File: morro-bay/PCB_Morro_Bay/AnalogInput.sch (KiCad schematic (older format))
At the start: 50 parts, among them U5 LM2902, U6 LM2902, U7 LM2902, U8 LM2902, U9 LM2902

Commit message: Work on analog inputs and pin naming
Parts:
- removed unit 2 of U9
- removed unit 3 of U9
- removed unit 4 of U9
- added D1, D10, D11, D12, D13, D14, D15, D16, D17, D18, D19, D2, D20, D3, D4, D5, D6, D7, D8, D9: 3.3V, symbol Device:D_Zener
- added R49, R51, R57, R59, R63, R65: 51.1K, symbol Device:R_US
- added R50, R52, R58, R60, R64, R66: 100K, symbol Device:R_US
- added R53, R54, R55, R56, R61, R62, R67, R68: 1K, symbol Device:R_US
- added SW1, SW10, SW11, SW12, SW13, SW14, SW15, SW16, SW17, SW18, SW19, SW2, SW20, SW3, SW4, SW5, SW6, SW7, SW8, SW9: SW_SPST, symbol Switch:SW_SPST
- added U10, U11, U12: LM2902, symbol Amplifier_Operational:LM2902
- R10, R12, R14, R16, R22, R24, R26, R28, R34, R36, R38, R40, R46, R48: value 10K -> 100K
- R11, R13, R15, R21, R23, R25, R27, R33, R35, R37, R39, R45, R47, R9: value 5.1K -> 51.1K
- R17, R19, R29, R31, R41, R43: value 5.1K -> 1K; Tolerance 0.1% -> (none)
- R18, R20, R30, R32, R42, R44: value 10K -> 1K; Tolerance 0.1% -> (none)
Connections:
- net labels added: 3V3_IN_1, 3V3_IN_10, 3V3_IN_11, 3V3_IN_12, 3V3_IN_13, 3V3_IN_14, 3V3_IN_15, 3V3_IN_16, 3V3_IN_17, 3V3_IN_18, 3V3_IN_19, 3V3_IN_2, 3V3_IN_20, 3V3_IN_3, 3V3_IN_4, 3V3_IN_5, 3V3_IN_6, 3V3_IN_7, 3V3_IN_8, 3V3_IN_9, 5V_IN_10, 5V_IN_11, 5V_IN_12, 5V_IN_13, 5V_IN_14, 5V_IN_15, 5V_IN_16, 5V_IN_17, 5V_IN_18, 5V_IN_19, 5V_IN_20, 5V_IN_5, 5V_IN_6, 5V_IN_7, 5V_IN_8, 5V_IN_9, IN_10_BUFFERED, IN_11_BUFFERED, IN_12_BUFFERED, IN_13_BUFFERED, IN_14_BUFFERED, IN_15_BUFFERED, IN_16_BUFFERED, IN_17_BUFFERED, IN_18_BUFFERED, IN_19_BUFFERED, IN_1_BUFFERED, IN_20_BUFFERED, IN_2_BUFFERED, IN_3_BUFFERED, IN_4_BUFFERED, IN_5_BUFFERED, IN_6_BUFFERED, IN_7_BUFFERED, IN_8_BUFFERED, IN_9_BUFFERED, SAMD_ADC_10, SAMD_ADC_11, SAMD_ADC_12, SAMD_ADC_13, SAMD_ADC_14, SAMD_ADC_15, SAMD_ADC_16, SAMD_ADC_17, SAMD_ADC_18, SAMD_ADC_19, SAMD_ADC_20, SAMD_ADC_5, SAMD_ADC_6, SAMD_ADC_7, SAMD_ADC_8, SAMD_ADC_9
- wire segments 220 -> 380
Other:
- moved on the sheet: R10, R9, U5A

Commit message: Add input connectors, DIP switches
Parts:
- removed SW1, SW10, SW11, SW12, SW13, SW14, SW15, SW16, SW17, SW18, SW19, SW2, SW20, SW3, SW4, SW5, SW6, SW7, SW8, SW9: SW_SPST, symbol Switch:SW_SPST
- added SW1, SW2: SW_DIP_x10, symbol Switch:SW_DIP_x10
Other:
- note added: "Analog Connectors"
- moved on the sheet: C22, C23, C24, C25, C26, D1, D10, D11, D12, D13, D14, D15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

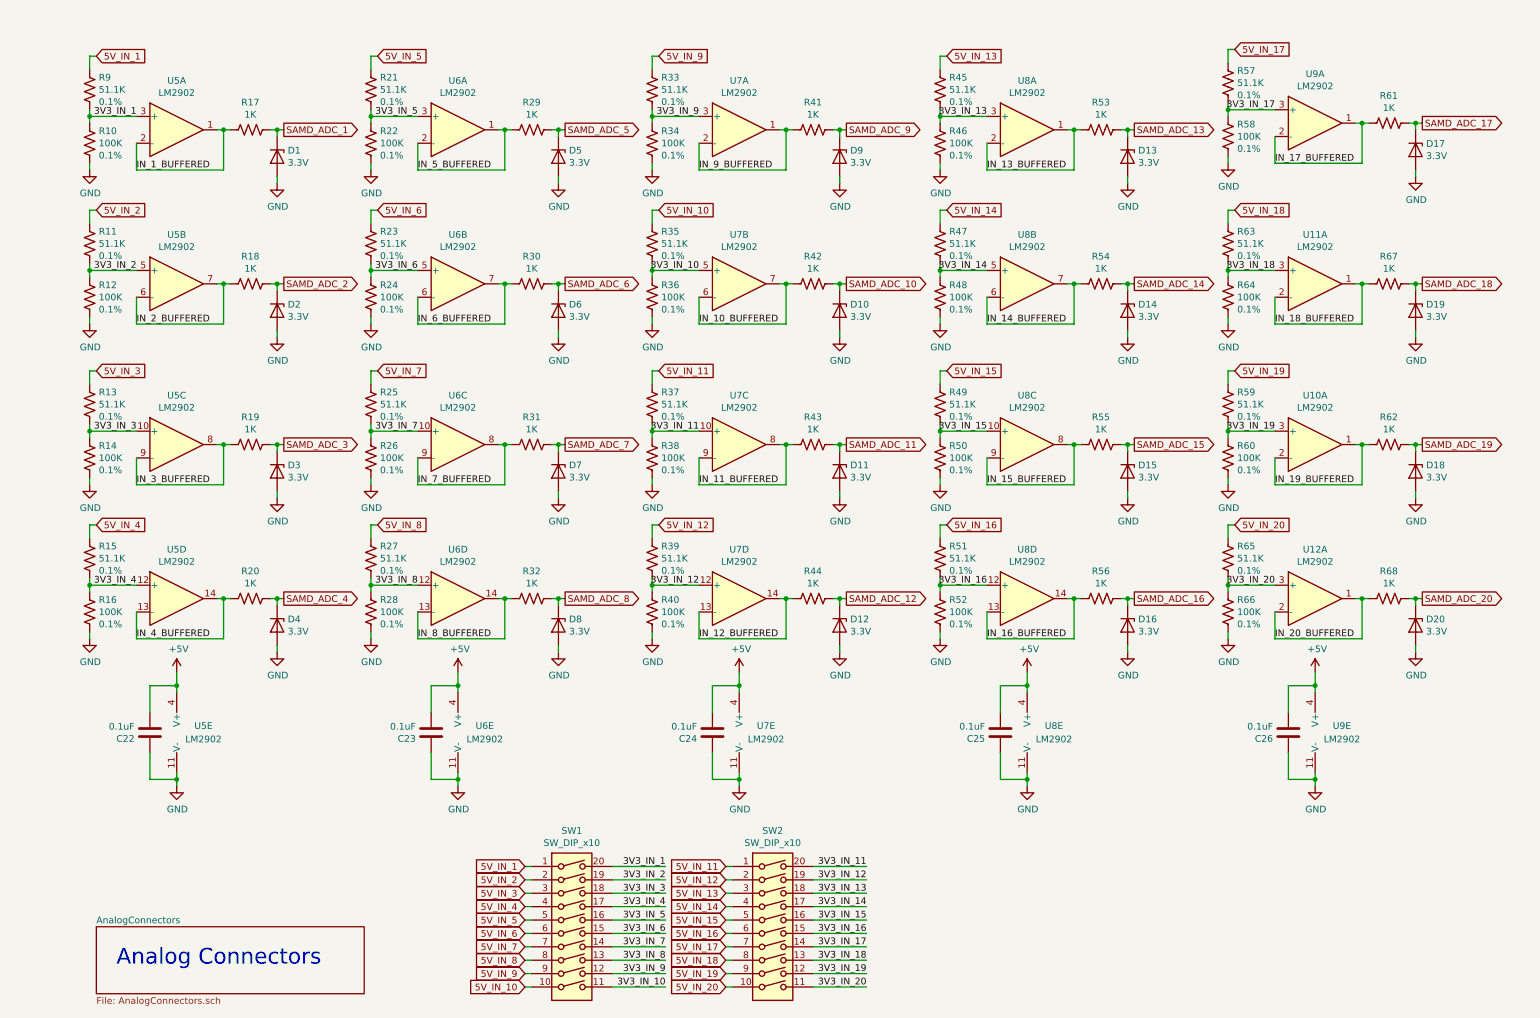
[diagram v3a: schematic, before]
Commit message: Switch to DC-DC reg
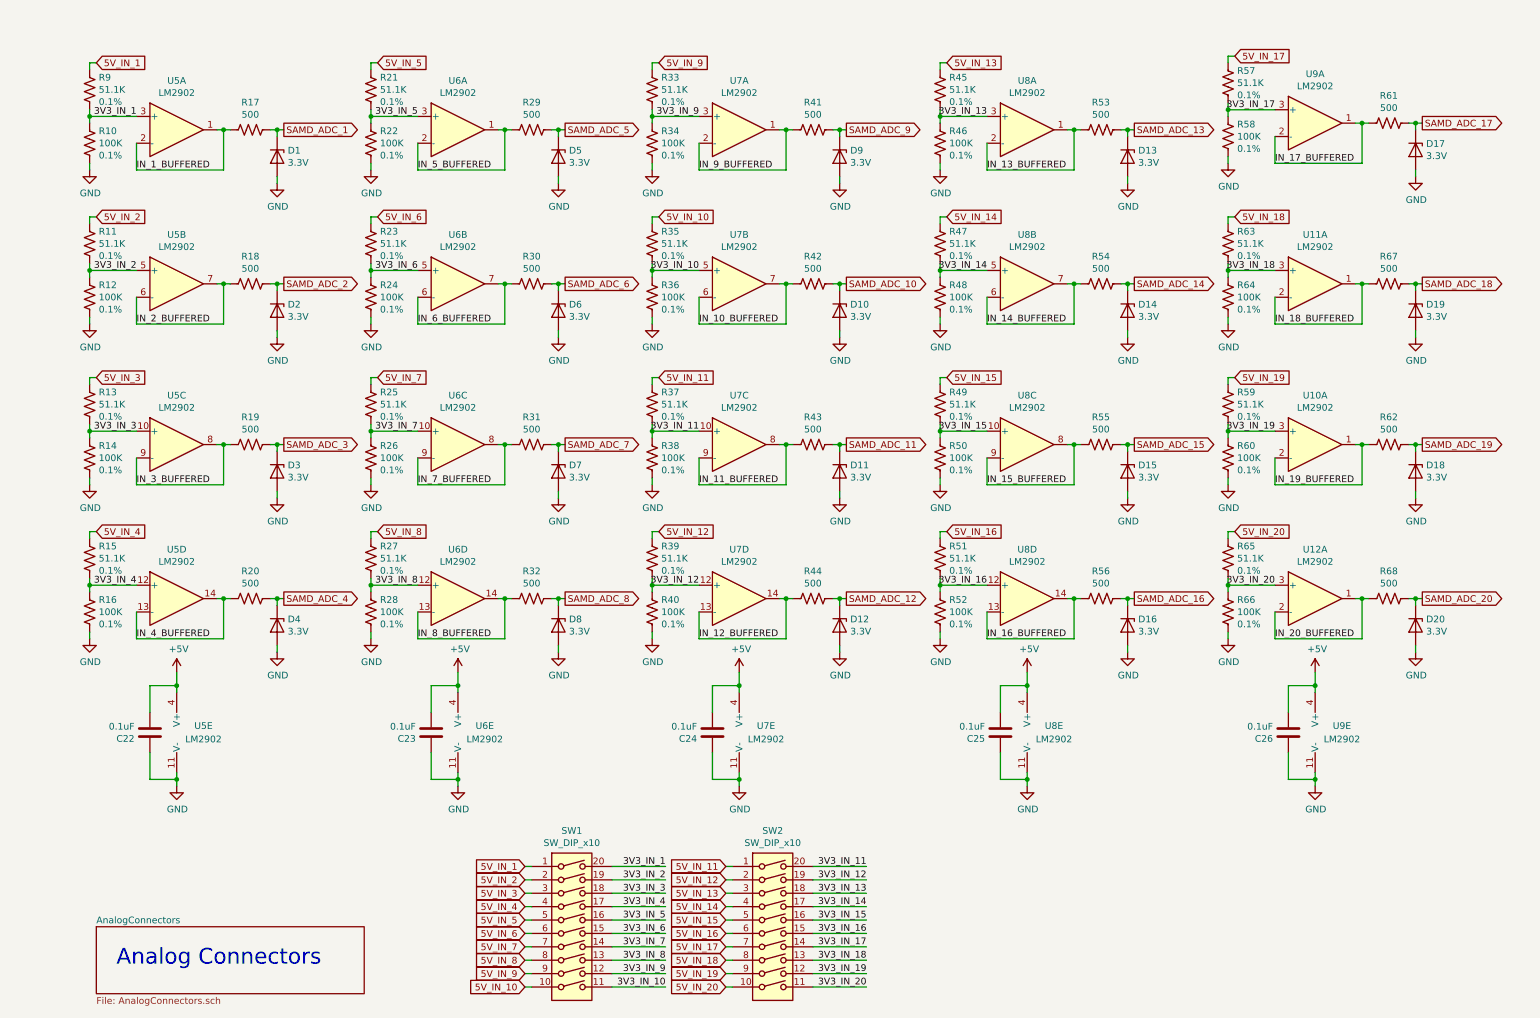
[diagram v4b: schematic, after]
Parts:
- R17, R18, R19, R20, R29, R30, R31, R32, R41, R42, R43, R44, R53, R54, R55, R56, R61, R62, R67, R68: value 1K -> 500

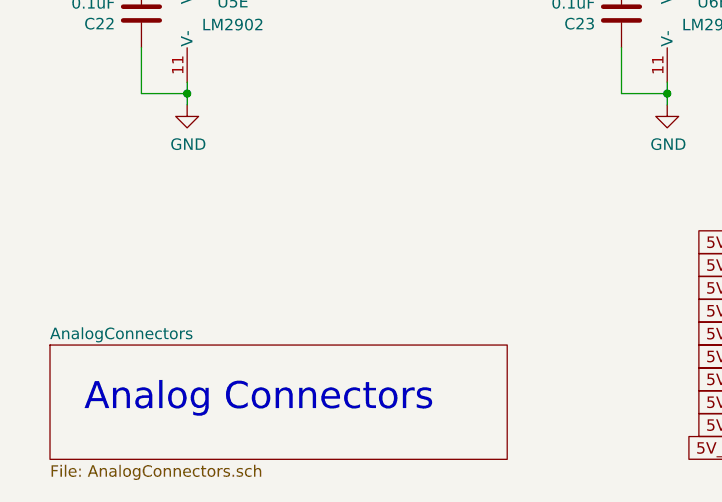
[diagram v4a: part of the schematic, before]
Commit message: Add external ADC
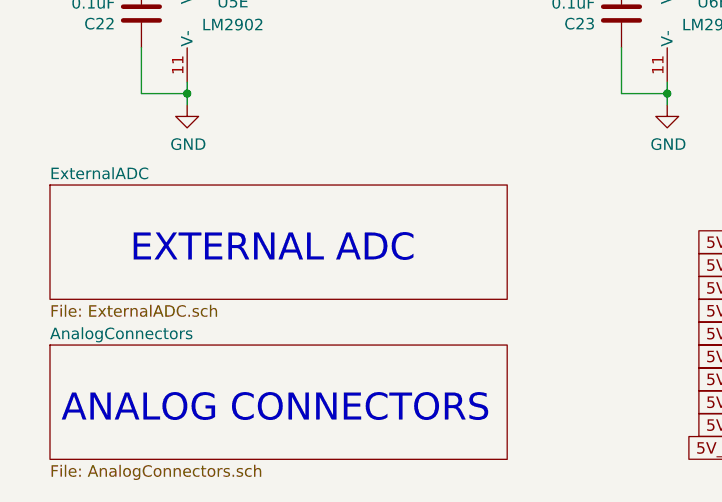
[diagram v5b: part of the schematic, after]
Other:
- note added: "ANALOG CONNECTORS"
- note added: "EXTERNAL ADC"
- note removed: "Analog Connectors"
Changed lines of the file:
@@
 $Descr A4 11693 8268
 encoding utf-8
-Sheet 2 3
+Sheet 2 4
 Title "Morro Bay Data Acquisition Board"
 Date ""
@@
 F1 "AnalogConnectors.sch" 50
 $EndSheet
-Text Notes 800  7400 0    118  ~ 0
-Analog Connectors
+Text Notes 700  7450 0    118  ~ 0
+ANALOG CONNECTORS
 $Comp
 L Switch:SW_DIP_x10 SW1
@@
 Wire Wire Line
 	5350 7550 5400 7550
+$Sheet
+S 650  6400 2000 500
+U 5E5467E7
+F0 "ExternalADC" 50
+F1 "ExternalADC.sch" 50
+$EndSheet
+Text Notes 1000 6750 0    118  ~ 0
+EXTERNAL ADC
 $EndSCHEMATC

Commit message: Ready for initial sch review
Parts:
- added C? (x2): 22uF, symbol Device:CP1
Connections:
- net +5V: now also C?.1, C?.1
- net GND: now also C?.2, C?.2
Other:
- moved on the sheet: SW1, SW2

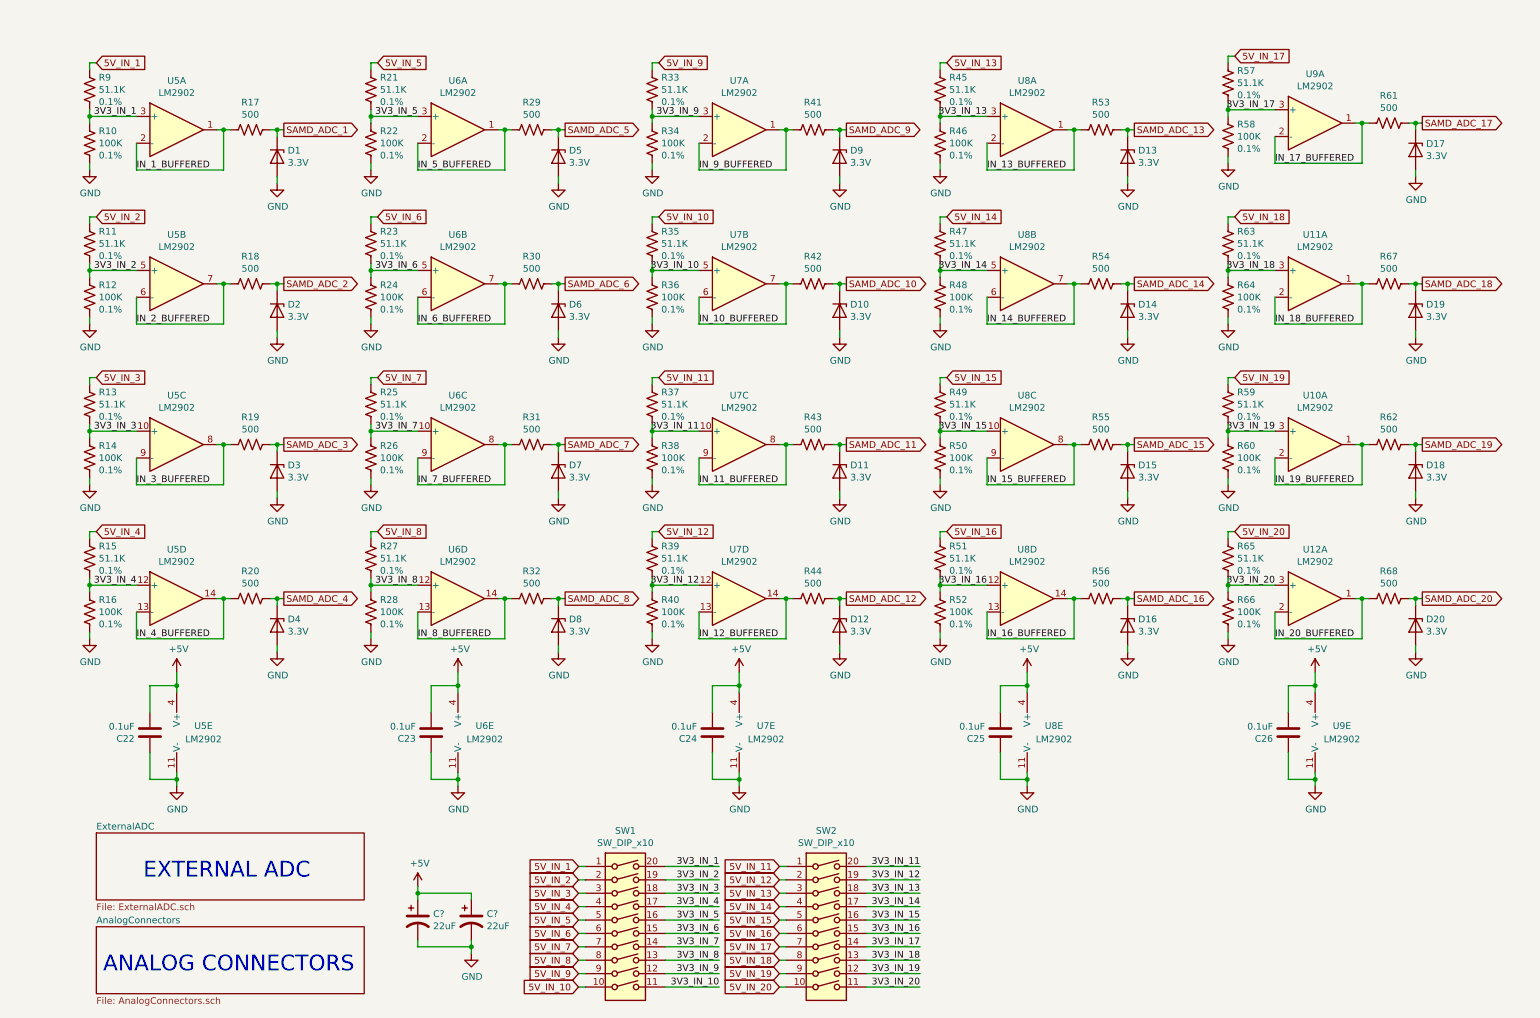
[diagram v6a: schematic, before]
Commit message: Work on BOM
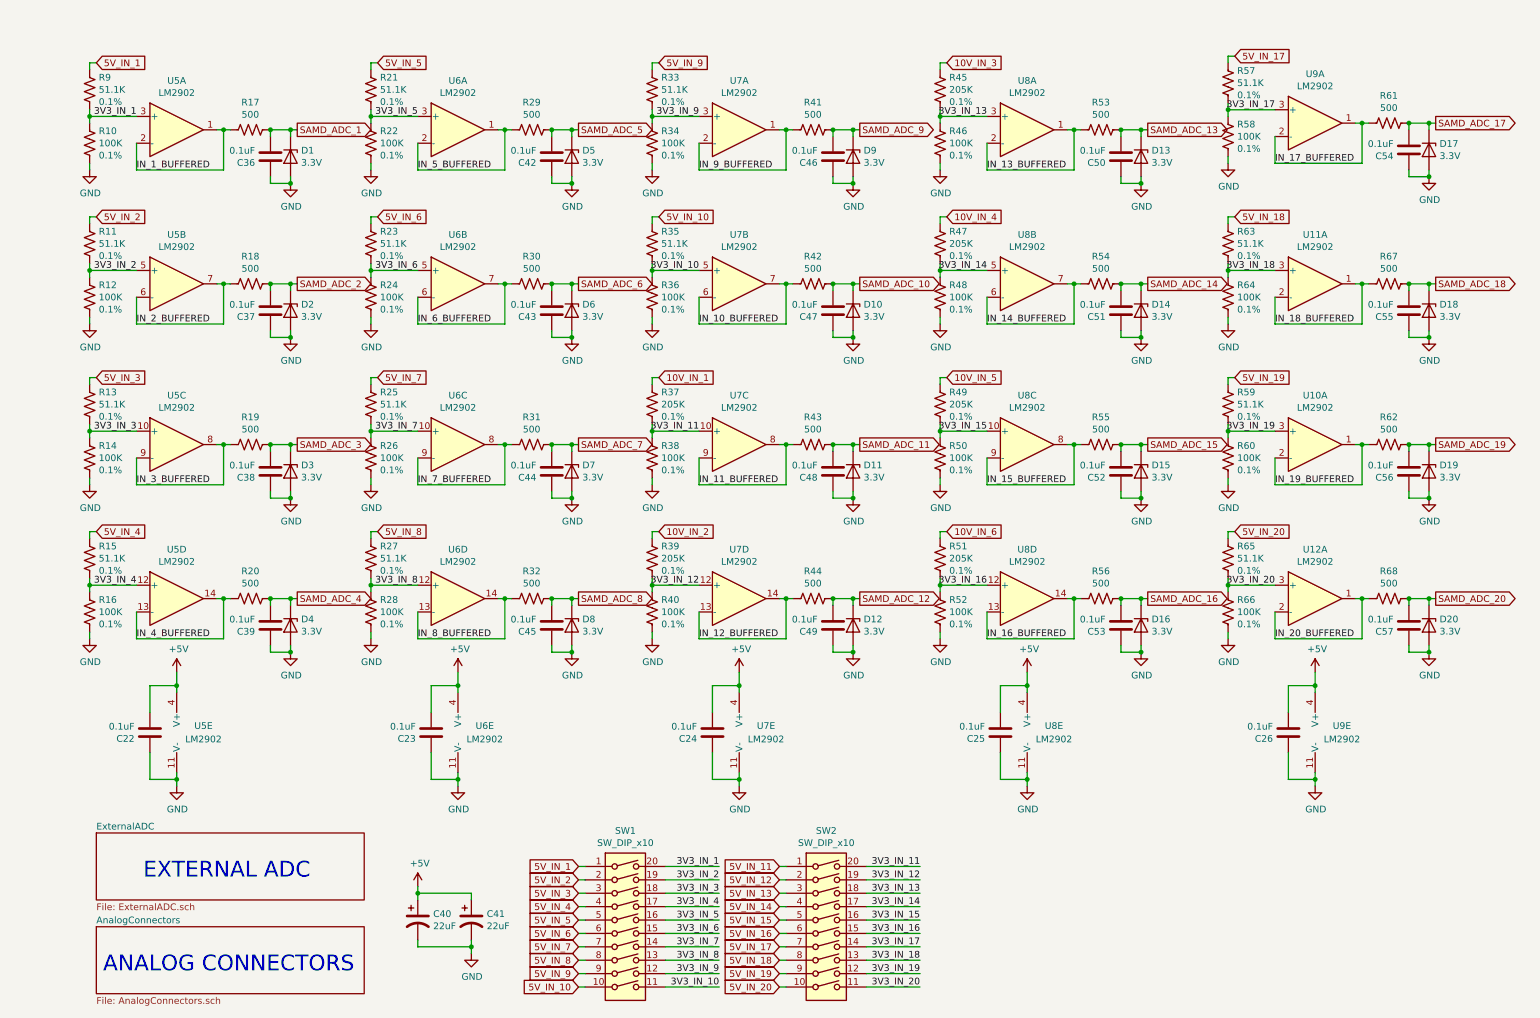
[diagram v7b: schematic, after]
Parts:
- added C36, C37, C38, C39, C42, C43, C44, C45, C46, C47, C48, C49, C50, C51, C52, C53, C54, C55, C56, C57: 0.1uF, Capacitor_SMD:C_0603_1608Metric_Pad1.05x0.95mm_HandSolder, symbol Device:C
- C22, C23, C24, C25, C26: footprint (none) -> Capacitor_SMD:C_0603_1608Metric_Pad1.05x0.95mm_HandSolder; Digikey (none) -> https://www.digikey.ca/product-detail/en/yageo/CC0603KRX7R8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; Part Number (none) -> CC0603KRX7R8BB104
- D1, D10, D11, D12, D13, D14, D15, D16, D17, D18, D19, D2, D20, D3, D4, D5, D6, D7, D8, D9: footprint (none) -> Diode_SMD:D_SOD-323_HandSoldering; Digikey (none) -> https://www.digikey.ca/product-detail/en/on-semiconductor/M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; Part Number (none) -> MM3Z3V3ST1G
- R37, R39, R45, R47, R49, R51: value 51.1K -> 205K
- gave numbers to parts that had none: 2
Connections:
- net 5V_IN_11: no longer R37.1
- net 5V_IN_12: no longer R39.1
- net 5V_IN_13: no longer R45.1
- net 5V_IN_14: no longer R47.1
- net 5V_IN_15: no longer R49.1
- net 5V_IN_16: no longer R51.1
- net GND: now also C36.1, C37.1, C38.1, C39.1, C42.1, C43.1, C44.1, C45.1, C46.1, C47.1, C48.1, C49.1, C50.1, C51.1, C52.1, C53.1, C54.1, C55.1, C56.1, C57.1
- net SAMD_ADC_1: now also C36.2
- net SAMD_ADC_10: now also C47.2
- net SAMD_ADC_11: now also C48.2
- net SAMD_ADC_12: now also C49.2
- net SAMD_ADC_13: now also C50.2
- net SAMD_ADC_14: now also C51.2
- net SAMD_ADC_15: now also C52.2
- net SAMD_ADC_16: now also C53.2
- net SAMD_ADC_17: now also C54.2
- net SAMD_ADC_18: now also D18.1 (K), C55.2; no longer D19.1 (K)
- net SAMD_ADC_19: now also D19.1 (K), C56.2; no longer D18.1 (K)
- net SAMD_ADC_2: now also C37.2
- net SAMD_ADC_20: now also C57.2
- net SAMD_ADC_3: now also C38.2
- net SAMD_ADC_4: now also C39.2
- net SAMD_ADC_5: now also C42.2
- net SAMD_ADC_6: now also C43.2
- net SAMD_ADC_7: now also C44.2
- net SAMD_ADC_8: now also C45.2
- net SAMD_ADC_9: now also C46.2
- new net 10V_IN_1: R37.1
- new net 10V_IN_2: R39.1
- new net 10V_IN_3: R45.1
- new net 10V_IN_4: R47.1
- new net 10V_IN_5: R49.1
- new net 10V_IN_6: R51.1
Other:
- moved on the sheet: D1

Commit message: More BOM
And if that don't work, use more gun.
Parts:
- removed C40, C41: 22uF, symbol Device:CP1
- added C40, C41: 22uF, Capacitor_SMD:C_0805_2012Metric_Pad1.15x1.40mm_HandSolder, symbol Device:C
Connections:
- net +5V: now also C40.1, C41.1
- net GND: now also C40.2, C41.2
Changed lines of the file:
@@
-	1    0    0    -1
-$EndComp
-$Comp
-L Device:CP1 C40
-U 1 1 5EEAB869
-P 3050 7050
-F 0 "C40" H 3165 7096 50  0000 L CNN
-F 1 "22uF" H 3165 7005 50  0000 L CNN
-F 2 "" H 3050 7050 50  0001 C CNN
-F 3 "~" H 3050 7050 50  0001 C CNN
-	1    3050 7050
-	1    0    0    -1
-$EndComp
-$Comp
-L Device:CP1 C41
-U 1 1 5EEAD276
-P 3450 7050
-F 0 "C41" H 3565 7096 50  0000 L CNN
-F 1 "22uF" H 3565 7005 50  0000 L CNN
-F 2 "" H 3450 7050 50  0001 C CNN
-F 3 "~" H 3450 7050 50  0001 C CNN
-	1    3450 7050
 	1    0    0    -1
 $EndComp
@@
 	-1   0    0    1
 $EndComp
+$Comp
+L Device:C C?
+U 1 1 5E78EDE6
+P 3050 7050
+AR Path="/5E78EDE6" Ref="C?"  Part="1"
+AR Path="/5E59A680/5E78EDE6" Ref="C40"  Part="1"
+F 0 "C40" H 3165 7096 50  0000 L CNN
+F 1 "22uF" H 3165 7005 50  0000 L CNN
+F 2 "Capacitor_SMD:C_0805_2012Metric_Pad1.15x1.40mm_HandSolder" H 3088 6900 50  0001 C CNN
+F 3 "~" H 3050 7050 50  0001 C CNN
+F 4 "CL21A226MAQNNNE" H 3050 7050 50  0001 C CNN "Part Number"
+F 5 "https://www.digikey.ca/product-detail/en/samsung-electro-mechanics/CL21A226MAQNNNE/1276-2908-1-ND/3890994" H 3050 7050 50  0001 C CNN "Digikey"
+	1    3050 7050
+	1    0    0    -1
+$EndComp
+$Comp
+L Device:C C?
+U 1 1 5E7BDB3E
+P 3450 7050
+AR Path="/5E7BDB3E" Ref="C?"  Part="1"
+AR Path="/5E59A680/5E7BDB3E" Ref="C41"  Part="1"
+F 0 "C41" H 3565 7096 50  0000 L CNN
+F 1 "22uF" H 3565 7005 50  0000 L CNN
+F 2 "Capacitor_SMD:C_0805_2012Metric_Pad1.15x1.40mm_HandSolder" H 3488 6900 50  0001 C CNN
+F 3 "~" H 3450 7050 50  0001 C CNN
+F 4 "CL21A226MAQNNNE" H 3450 7050 50  0001 C CNN "Part Number"
+F 5 "https://www.digikey.ca/product-detail/en/samsung-electro-mechanics/CL21A226MAQNNNE/1276-2908-1-ND/3890994" H 3450 7050 50  0001 C CNN "Digikey"
+	1    3450 7050
+	1    0    0    -1
+$EndComp
 $EndSCHEMATC
